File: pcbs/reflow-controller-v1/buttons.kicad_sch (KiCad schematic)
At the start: 16 parts, among them SW1001 TS04-66-85-BK-160-SMT, SW1003 TS04-66-85-BK-160-SMT, SW101 PEC12R-3220F-S0024

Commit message: added temp sensor
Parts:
- renumbered SW101 to SW1002
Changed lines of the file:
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@@
   (symbol (lib_id "Device:RotaryEncoder_Switch") (at 58.42 96.52 0) (mirror y) (unit 1)
     (in_bom yes) (on_board yes) (dnp no) (fields_autoplaced)
-    (property "Reference" "SW101" (at 58.42 86.36 0)
+    (property "Reference" "SW1002" (at 58.42 86.36 0)
       (effects (font (size 1.27 1.27)))
     )
@@
     (instances
       (project "reflow-controller-v1"
-        (path "/843848ae-bf49-42cb-8f8b-76790d2e568d"
-          (reference "SW101") (unit 1)
-        )
         (path "/843848ae-bf49-42cb-8f8b-76790d2e568d/732d703e-e996-4cd3-add9-becac623524e"
           (reference "SW1002") (unit 1)

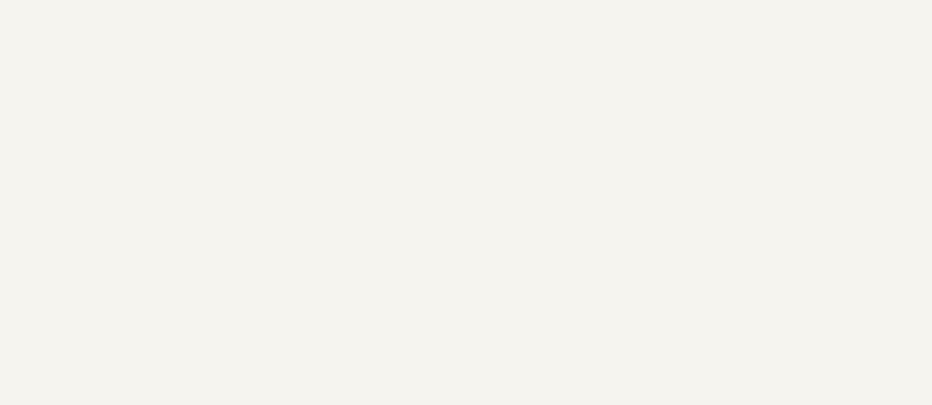
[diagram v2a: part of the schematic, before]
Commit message: footprint assignement fixed; buzzer added
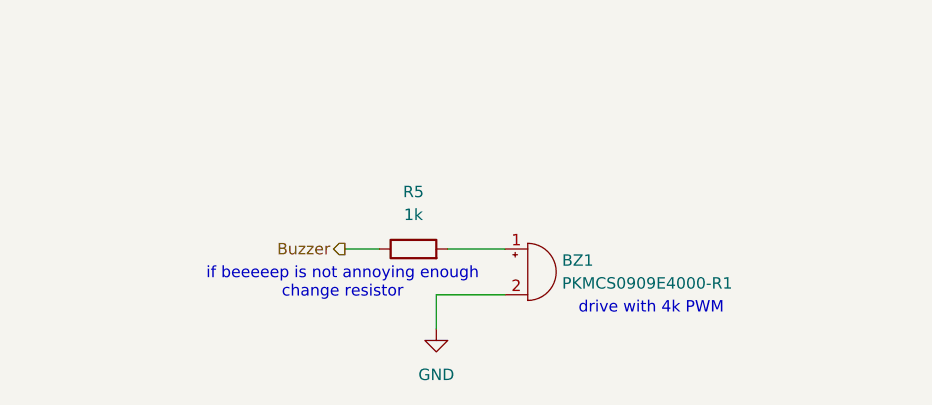
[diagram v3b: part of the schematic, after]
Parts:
- added BZ1: PKMCS0909E4000-R1, Buzzer_Beeper:Buzzer_Murata_PKMCS0909E, symbol Device:Buzzer
- added R5: 1k, symbol Device:R
- SW1002: footprint Rotary_Encoder:RotaryEncoder_Bourns_Vertical_PEC12R-3xxxF-Sxxxx -> Rotary_Encoder:RotaryEncoder_Bourns_Vertical_PEC12R-3x17F-Sxxxx
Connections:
- net GND: now also BZ1.2 (-)
- new net: BZ1.1 (+), R5.2
- new net Buzzer: R5.1
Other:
- note added: "drive with 4k PWM"
- note added: "if beeeeep is not annoying enough change resistor"

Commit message: [pcbs] Add initial placement
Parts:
- R5: footprint (none) -> Resistor_SMD:R_0603_1608Metric
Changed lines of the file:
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@@
 			)
 		)
-		(property "Footprint" ""
+		(property "Footprint" "Resistor_SMD:R_0603_1608Metric"
 			(at 110.49 155.448 90)
 			(effects
